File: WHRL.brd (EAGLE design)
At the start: 33 x 29.2 mm, 23 parts, among them IC1 CD4049UBE

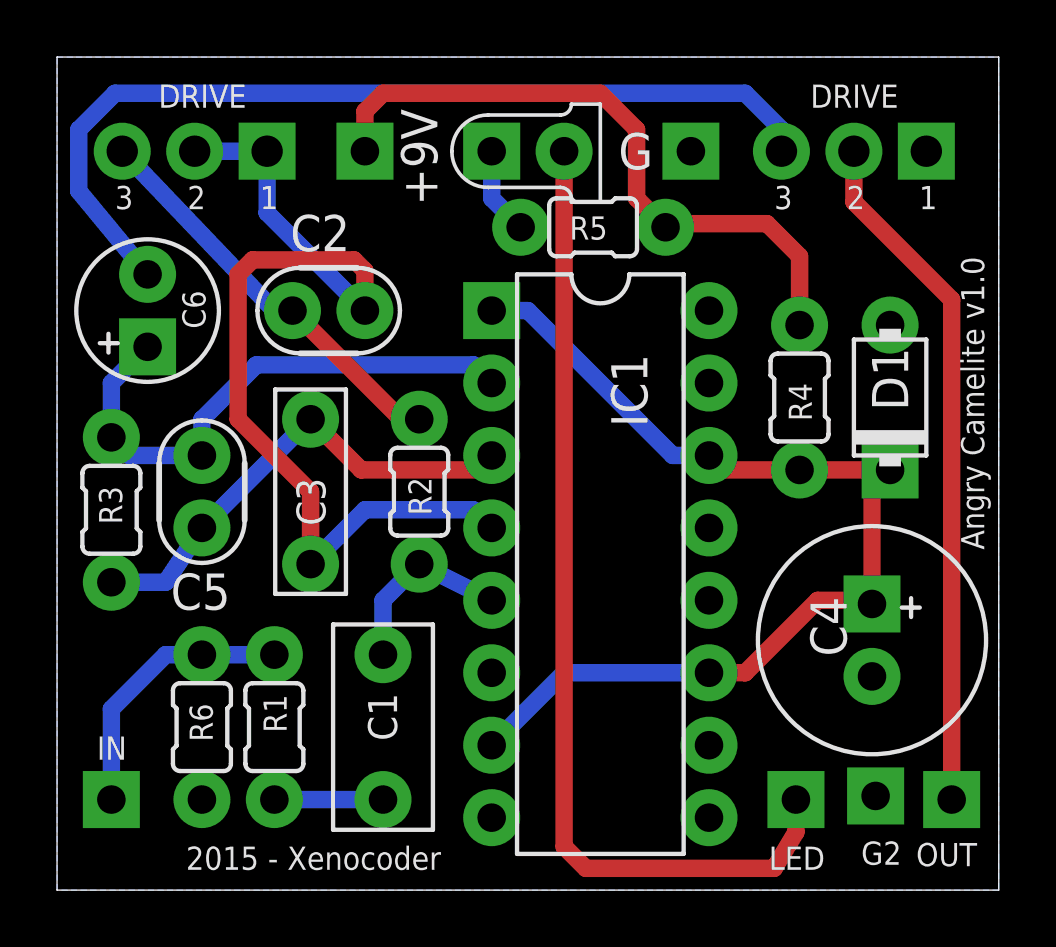
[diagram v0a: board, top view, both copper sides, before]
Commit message: Rotated pots to right direction and rerouted traces. V1.1
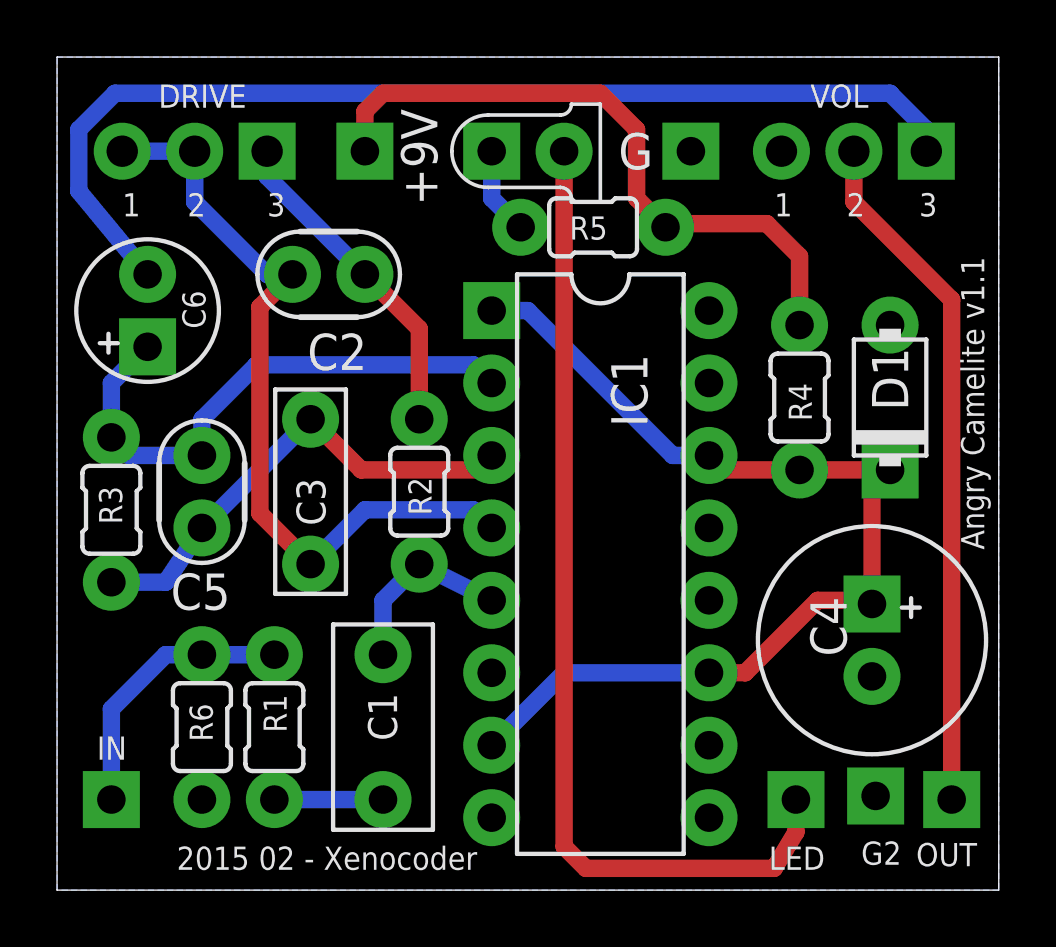
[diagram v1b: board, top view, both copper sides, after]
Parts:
- moved C2 1.27 mm to (9.53, 21.6), turned to 180 degrees
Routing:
- net N$6: track 34.4 -> 27.6 mm
- net N$9: track 32.4 -> 37.5 mm
- net N$11: track 14.4 -> 11.6 mm
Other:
- board text added: "1"
- board text added: "2"
- board text added: "2015 02 - Xenocoder"
- board text added: "3"
- board text added: "Angry Camelite v1.1"
- board text added: "VOL"
- board text removed: "2015 - Xenocoder"
- board text removed: "Angry Camelite v1.0"
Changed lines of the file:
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@@
 <wire x1="33.02" y1="29.21" x2="0" y2="29.21" width="0" layer="20"/>
 <wire x1="0" y1="29.21" x2="0" y2="0" width="0" layer="20"/>
-<text x="32.512" y="11.938" size="0.8128" layer="25" rot="R90">Angry Camelite v1.0</text>
-<text x="13.462" y="1.524" size="0.8128" layer="25" rot="R180">2015 - Xenocoder</text>
+<text x="32.512" y="11.938" size="0.8128" layer="25" rot="R90">Angry Camelite v1.1</text>
+<text x="14.732" y="1.524" size="0.8128" layer="25" rot="R180">2015 02 - Xenocoder</text>
 <text x="3.556" y="27.432" size="0.8128" layer="25">DRIVE</text>
-<text x="26.416" y="27.432" size="0.8128" layer="25">DRIVE</text>
+<text x="26.416" y="27.432" size="0.8128" layer="25">VOL</text>
+<text x="2.286" y="23.622" size="0.8128" layer="25" font="vector">1</text>
+<text x="4.572" y="23.622" size="0.8128" layer="25" font="vector">2</text>
+<text x="7.366" y="23.622" size="0.8128" layer="25" font="vector">3</text>
+<text x="25.146" y="23.622" size="0.8128" layer="25" font="vector">1</text>
+<text x="30.226" y="23.622" size="0.8128" layer="25" font="vector">3</text>
+<text x="27.686" y="23.622" size="0.8128" layer="25" font="vector">2</text>
 </plain>
 <attributes>
@@
 <attribute name="NAME" x="9.413" y="12.777" size="1.016" layer="25" ratio="12" rot="R90"/>
 </element>
-<element name="C2" library="mb_caps-ceramic" package="050X030_025" value="51pF" x="9.525" y="20.32" smashed="yes">
-<attribute name="NAME" x="8.1788" y="22.4028" size="1.27" layer="25" ratio="12"/>
+<element name="C2" library="mb_caps-ceramic" package="050X030_025" value="51pF" x="9.525" y="21.59" smashed="yes" rot="R180">
+<attribute name="NAME" x="10.8712" y="19.5072" size="1.27" layer="25" ratio="12" rot="R180"/>
 </element>
 <element name="C5" library="mb_caps-ceramic" package="050X030_025" value="100pF" x="5.08" y="13.97" smashed="yes" rot="R90">
@@
 <contactref element="DRIVE" pad="P$1"/>
 <contactref element="DRIVE" pad="P$2"/>
-<wire x1="4.826" y1="25.908" x2="7.366" y2="25.908" width="0.6096" layer="16"/>
 <wire x1="8.89" y1="11.43" x2="10.795" y2="13.335" width="0.6096" layer="16"/>
 <wire x1="10.795" y1="13.335" x2="14.605" y2="13.335" width="0.6096" layer="16"/>
 <wire x1="14.605" y1="13.335" x2="15.24" y2="12.7" width="0.6096" layer="16"/>
-<wire x1="10.795" y1="20.32" x2="7.366" y2="23.749" width="0.6096" layer="16"/>
-<wire x1="7.366" y1="23.749" x2="7.366" y2="25.908" width="0.6096" layer="16"/>
-<wire x1="10.795" y1="20.32" x2="10.795" y2="21.717" width="0.6096" layer="1"/>
-<wire x1="10.795" y1="21.717" x2="10.414" y2="22.098" width="0.6096" layer="1"/>
-<wire x1="10.414" y1="22.098" x2="6.858" y2="22.098" width="0.6096" layer="1"/>
-<wire x1="6.858" y1="22.098" x2="6.35" y2="21.59" width="0.6096" layer="1"/>
-<wire x1="6.35" y1="21.59" x2="6.35" y2="16.51" width="0.6096" layer="1"/>
-<wire x1="6.35" y1="16.51" x2="8.89" y2="13.97" width="0.6096" layer="1"/>
-<wire x1="8.89" y1="13.97" x2="8.89" y2="11.43" width="0.6096" layer="1"/>
+<wire x1="2.286" y1="25.908" x2="4.826" y2="25.908" width="0.6096" layer="16"/>
+<wire x1="8.255" y1="21.59" x2="7.366" y2="21.59" width="0.6096" layer="16"/>
+<wire x1="7.366" y1="21.59" x2="4.826" y2="24.13" width="0.6096" layer="16"/>
+<wire x1="4.826" y1="24.13" x2="4.826" y2="25.908" width="0.6096" layer="16"/>
+<wire x1="8.255" y1="21.59" x2="7.112" y2="20.447" width="0.6096" layer="1"/>
+<wire x1="7.112" y1="20.447" x2="7.112" y2="13.208" width="0.6096" layer="1"/>
+<wire x1="7.112" y1="13.208" x2="8.89" y2="11.43" width="0.6096" layer="1"/>
 </signal>
 <signal name="N$7">
@@
 <wire x1="0.762" y1="24.511" x2="0.762" y2="26.67" width="0.6096" layer="16"/>
 <wire x1="0.762" y1="26.67" x2="2.032" y2="27.94" width="0.6096" layer="16"/>
-<wire x1="2.032" y1="27.94" x2="24.13" y2="27.94" width="0.6096" layer="16"/>
-<wire x1="24.13" y1="27.94" x2="25.4" y2="26.67" width="0.6096" layer="16"/>
-<wire x1="25.4" y1="25.908" x2="25.4" y2="26.67" width="0.6096" layer="16"/>
+<wire x1="2.032" y1="27.94" x2="29.21" y2="27.94" width="0.6096" layer="16"/>
+<wire x1="30.48" y1="25.908" x2="30.48" y2="26.67" width="0.6096" layer="16"/>
+<wire x1="30.48" y1="26.67" x2="29.21" y2="27.94" width="0.6096" layer="16"/>
 </signal>
 <signal name="N$10">
@@
 <contactref element="C2" pad="1"/>
 <contactref element="DRIVE" pad="P$3"/>
-<wire x1="8.255" y1="20.32" x2="7.62" y2="20.32" width="0.6096" layer="16"/>
-<wire x1="7.62" y1="20.32" x2="2.286" y2="25.908" width="0.6096" layer="16"/>
-<wire x1="12.7" y1="16.51" x2="12.065" y2="16.51" width="0.6096" layer="1"/>
-<wire x1="12.065" y1="16.51" x2="8.255" y2="20.32" width="0.6096" layer="1"/>
+<wire x1="10.795" y1="21.59" x2="7.366" y2="25.019" width="0.6096" layer="16"/>
+<wire x1="7.366" y1="25.019" x2="7.366" y2="25.908" width="0.6096" layer="16"/>
+<wire x1="12.7" y1="16.51" x2="12.7" y2="19.685" width="0.6096" layer="1"/>
+<wire x1="12.7" y1="19.685" x2="10.795" y2="21.59" width="0.6096" layer="1"/>
 </signal>
 <signal name="IN">
